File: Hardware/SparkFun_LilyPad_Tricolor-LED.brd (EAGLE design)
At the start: 20 x 20 mm, 11 parts

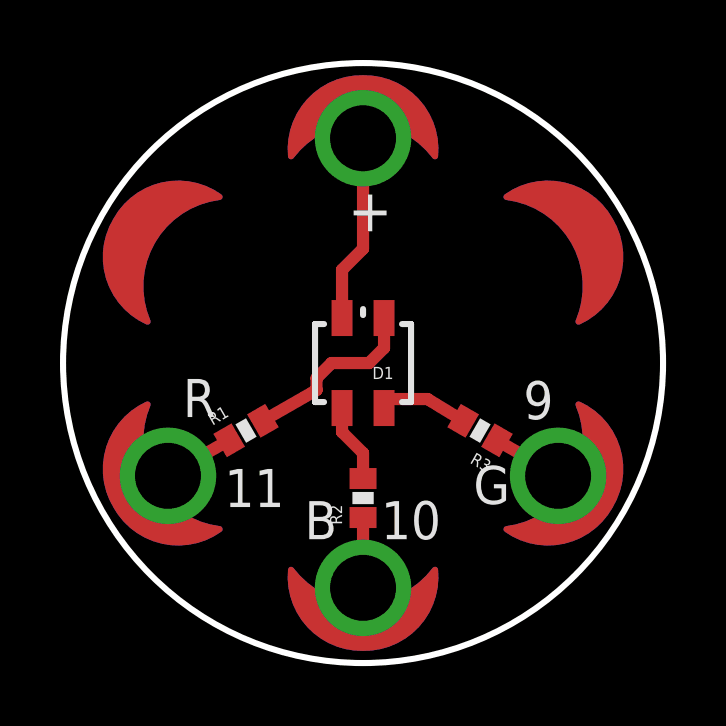
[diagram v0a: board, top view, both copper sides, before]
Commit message: Changed to common cathode LED, changed resistors
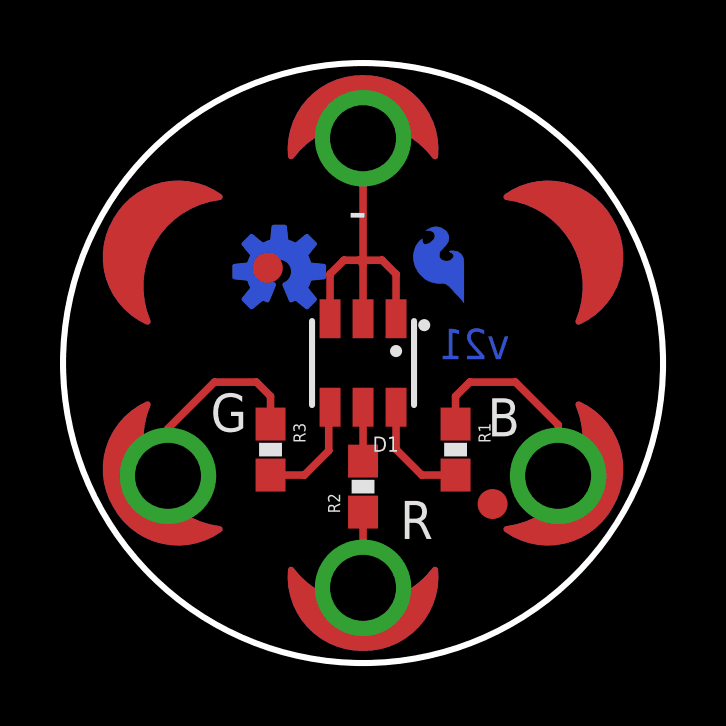
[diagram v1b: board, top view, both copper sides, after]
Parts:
- added FID1, FID2: FIDUCIAL1X2, SparkFun-Aesthetics:FIDUCIAL-1X2
- added FRAME1: (no value), SparkFun-Aesthetics:CREATIVE_COMMONS
- added LOGO1: OSHW-LOGOS-COPPER, SparkFun-Aesthetics:OSHW-LOGO-S_COPPER
- added LOGO2: SFE_LOGO_FLAME.1COP, SparkFun-Aesthetics:SFE_LOGO_FLAME_COPPER_.1
- D1: value LED-TRICOLOR -> LED-TRICOLOR-NO-COMPLCC-6-SMD; device SparkFun:LED-TRICOLOR-SMD -> SparkFun-LED:PLCC-6-LED
- R1: value 200 -> 20; device SparkFun:0402-RES -> SparkFun-Resistors:0603-RES
- R2: value 100 -> 82; device SparkFun:0402-RES -> SparkFun-Resistors:0603-RES
- R3: value 100 -> 20; device SparkFun:0402-RES -> SparkFun-Resistors:0603-RES
- moved R1 7.01 mm to (3.08, -2.88), turned to 270 degrees
- moved R3 7.01 mm to (-3.08, -2.88), turned to 270 degrees
- moved R2 0.38 mm to (0.00, -4.12)
- renumbered U$10 to GND, U$7 to GRN, U$8 to BLU, U$9 to RED
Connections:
- net B renamed N$2
- removed net +: D1.A, GND.1
- removed net G: BLU.1, R3.1
- removed net R: GRN.1, R1.1
- new net GND: D1.CB, D1.CG, D1.CR, GND.1
- new net N$1: BLU.1, R1.1
- new net N$3: GRN.1, R3.1
- net BLU: now also D1.AB, R1.2; no longer D1.B, R2.2
- net GRN: now also D1.AG; no longer D1.G
- net RED: now also D1.AR, R2.2; no longer D1.R, R1.2
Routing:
- net GND: track 0.00 -> 11.6 mm
- net N$1: track 0.00 -> 6.83 mm
- net N$3: track 0.00 -> 6.76 mm
- net +: track 6.41 -> 0.00 mm
- net RED: track 6.12 -> 1.79 mm
- net R: track 2.44 -> 0.00 mm
- net G: track 2.36 -> 0.00 mm
- net BLU: track 2.71 -> 3.74 mm
- net GRN: track 3.24 -> 3.74 mm
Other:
- board text added: "-"
- board text added: "Aaron Weiss"
- board text added: "Dimension in inches"
- board text added: "Revision by: Dia Campbell"
- board text added: "Thickness 0.8mm"
- board text added: "v21"
- board text removed: "+"
- board text removed: "10"
- board text removed: "11"
- board text removed: "9"

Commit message: Small schematic correction, fixed version number
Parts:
- added U$4: REVISION, SparkFun-Aesthetics:REVISION
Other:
- board text added: "Dia Campbell"
- board text added: "v20"
- board text removed: "Revision by: Dia Campbell"
- board text removed: "v21"
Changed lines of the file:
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@@
 <layer number="22" name="bPlace" color="14" fill="1" visible="yes" active="yes"/>
 <layer number="23" name="tOrigins" color="15" fill="1" visible="yes" active="yes"/>
-<layer number="24" name="bOrigins" color="15" fill="1" visible="no" active="yes"/>
+<layer number="24" name="bOrigins" color="15" fill="1" visible="yes" active="yes"/>
 <layer number="25" name="tNames" color="7" fill="1" visible="no" active="yes"/>
 <layer number="26" name="bNames" color="7" fill="1" visible="no" active="yes"/>
@@
 <vertex x="0" y="-8.2"/>
 </polygon>
-<text x="2.54" y="1.143" size="1.016" layer="16" font="vector" ratio="15" rot="MR180">v21</text>
+<text x="2.54" y="1.143" size="1.016" layer="16" font="vector" ratio="15" rot="MR180">v20</text>
 <text x="-67.945" y="-0.381" size="1.778" layer="51" font="vector" ratio="15">Aaron Weiss</text>
-<text x="-86.995" y="-3.302" size="1.778" layer="51" font="vector" ratio="15">Revision by: Dia Campbell</text>
+<text x="-67.945" y="-3.302" size="1.778" layer="51" font="vector" ratio="15">Dia Campbell</text>
 <dimension x1="10" y1="0" x2="-10" y2="0" x3="0" y3="-17.78" textsize="1.778" textratio="15" layer="51" dtype="diameter" unit="inch"/>
 <text x="-12.7" y="-25.4" size="1.778" layer="51" font="vector" ratio="15">Dimension in inches</text>
@@
 <element name="FID1" library="SparkFun-Aesthetics" package="FIDUCIAL-1X2" value="FIDUCIAL1X2" x="-3.175" y="3.175"/>
 <element name="FID2" library="SparkFun-Aesthetics" package="FIDUCIAL-1X2" value="FIDUCIAL1X2" x="4.318" y="-4.699"/>
+<element name="U$4" library="SparkFun-Aesthetics" package="REVISION" value="REVISION" x="-87.249" y="-3.048"/>
 </elements>
 <signals>
@@
 </signal>
 <signal name="GND">
-<contactref element="GND" pad="1"/>
 <contactref element="D1" pad="CR"/>
 <contactref element="D1" pad="CB"/>
@@
 <wire x1="0" y1="1.475" x2="0" y2="3.302" width="0.254" layer="1"/>
 <wire x1="0" y1="3.302" x2="0" y2="3.429" width="0.254" layer="1"/>
-<wire x1="0" y1="3.429" x2="0" y2="7.493" width="0.254" layer="1"/>
 <wire x1="-1.1" y1="1.475" x2="-1.1" y2="2.964" width="0.254" layer="1"/>
 <wire x1="-1.1" y1="2.964" x2="-0.635" y2="3.429" width="0.254" layer="1"/>
@@
 <wire x1="-0.635" y1="3.429" x2="-0.127" y2="3.429" width="0.254" layer="1"/>
 <wire x1="-0.127" y1="3.429" x2="0" y2="3.302" width="0.254" layer="1"/>
+<contactref element="GND" pad="1"/>
+<wire x1="0" y1="7.493" x2="0" y2="3.429" width="0.254" layer="1"/>
 </signal>
 <signal name="N$1">
